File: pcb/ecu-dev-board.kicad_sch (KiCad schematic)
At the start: 1 part, among them J1 MX23A18NF1

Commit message: added more connector tags
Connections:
- net MAP_SW: now reaches J1.14
- net COIL_QS: now reaches J1.16
- net +12V: now reaches J1.3
- net DIGITAL_QS_IN: now reaches J1.4
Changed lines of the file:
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@@
+	(wire
+		(pts
+			(xy 53.34 171.45) (xy 55.88 171.45)
+		)
+		(stroke
+			(width 0)
+			(type default)
+		)
+	)
 	(wire
 		(pts
@@
 	(wire
 		(pts
+			(xy 81.28 179.07) (xy 78.74 179.07)
+		)
+		(stroke
+			(width 0)
+			(type default)
+		)
+	)
+	(wire
+		(pts
+			(xy 46.99 168.91) (xy 55.88 168.91)
+		)
+		(stroke
+			(width 0)
+			(type default)
+		)
+	)
+	(wire
+		(pts
 			(xy 46.99 166.37) (xy 55.88 166.37)
 		)
@@
 	(wire
 		(pts
+			(xy 81.28 173.99) (xy 78.74 173.99)
+		)
+		(stroke
+			(width 0)
+			(type default)
+		)
+	)
+	(wire
+		(pts
 			(xy 81.28 166.37) (xy 78.74 166.37)
 		)
@@
 		)
 	)
+	(global_label "DIGITAL_QS_IN"
+		(shape input)
+		(at 53.34 171.45 180)
+		(fields_autoplaced yes)
+		(effects
+			(font
+				(size 1.27 1.27)
+			)
+			(justify right)
+		)
+		(property "Intersheetrefs" "${INTERSHEET_REFS}"
+			(at 37.1104 171.45 0)
+			(effects
+				(font
+					(size 1.27 1.27)
+				)
+				(justify right)
+				(hide yes)
+			)
+		)
+	)
 	(global_label "KILL_SWITCH"
 		(shape input)
@@
 		)
 	)
+	(global_label "COIL_QS"
+		(shape input)
+		(at 81.28 179.07 0)
+		(fields_autoplaced yes)
+		(effects
+			(font
+				(size 1.27 1.27)
+			)
+			(justify left)
+		)
+		(property "Intersheetrefs" "${INTERSHEET_REFS}"
+			(at 92.0062 179.07 0)
+			(effects
+				(font
+					(size 1.27 1.27)
+				)
+				(justify left)
+				(hide yes)
+			)
+		)
+	)
 	(global_label "COIL"
 		(shape input)
@@
 		(property "Intersheetrefs" "${INTERSHEET_REFS}"
 			(at 91.4014 168.91 0)
+			(effects
+				(font
+					(size 1.27 1.27)
+				)
+				(justify left)
+				(hide yes)
+			)
+		)
+	)
+	(global_label "MAP_SW"
+		(shape input)
+		(at 81.28 173.99 0)
+		(fields_autoplaced yes)
+		(effects
+			(font
+				(size 1.27 1.27)
+			)
+			(justify left)
+		)
+		(property "Intersheetrefs" "${INTERSHEET_REFS}"
+			(at 91.7037 173.99 0)
 			(effects
 				(font
@@
 					(unit 1)
 				)
+			)
+		)
+	)
+	(symbol
+		(lib_id "power:+12V")
+		(at 46.99 168.91 90)
+		(unit 1)
+		(exclude_from_sim no)
+		(in_bom yes)
+		(on_board yes)
+		(dnp no)
+		(fields_autoplaced yes)
+		(property "Reference" "#PWR059"
+			(at 50.8 168.91 0)
+			(effects
+				(font
+					(size 1.27 1.27)
+				)
+				(hide yes)
+			)
+		)
+		(property "Value" "+12V"
+			(at 43.18 168.9099 90)
+			(effects
+				(font
+					(size 1.27 1.27)
+				)
+				(justify left)
+			)
+		)
+		(property "Footprint" ""
+			(at 46.99 168.91 0)
+			(effects
+				(font
+					(size 1.27 1.27)
+				)
+				(hide yes)
+			)
+		)
+		(property "Datasheet" ""
+			(at 46.99 168.91 0)
+			(effects
+				(font
+					(size 1.27 1.27)
+				)
+				(hide yes)
+			)
+		)
+		(property "Description" "Power symbol creates a global label with name \"+12V\""
+			(at 46.99 168.91 0)
+			(effects
+				(font
+					(size 1.27 1.27)
+				)
+				(hide yes)
+			)
+		)
+		(pin "1"
+		)
+		(instances
+			(project ""
+				(path "/38d4df77-b5a0-4642-8410-8b13c21c2c3b"
+					(reference "#PWR059")
+					(unit 1)
+				)

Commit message: enhanced pickup simulation
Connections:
- net PICKUP_SIM+: now reaches J1.8
- net PICKUP_SIM-: now reaches J1.9
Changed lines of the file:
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@@
+	(wire
+		(pts
+			(xy 53.34 184.15) (xy 55.88 184.15)
+		)
+		(stroke
+			(width 0)
+			(type default)
+		)
+	)
 	(wire
 		(pts
@@
 	(wire
 		(pts
-			(xy 44.45 179.07) (xy 55.88 179.07)
+			(xy 38.1 179.07) (xy 55.88 179.07)
 		)
 		(stroke
@@
 	(wire
 		(pts
+			(xy 53.34 181.61) (xy 55.88 181.61)
+		)
+		(stroke
+			(width 0)
+			(type default)
+		)
+	)
+	(wire
+		(pts
 			(xy 81.28 173.99) (xy 78.74 173.99)
 		)
@@
 		)
 	)
+	(global_label "PICKUP_SIM+"
+		(shape input)
+		(at 53.34 181.61 180)
+		(fields_autoplaced yes)
+		(effects
+			(font
+				(size 1.27 1.27)
+			)
+			(justify right)
+		)
+		(property "Intersheetrefs" "${INTERSHEET_REFS}"
+			(at 37.5338 181.61 0)
+			(effects
+				(font
+					(size 1.27 1.27)
+				)
+				(justify right)
+				(hide yes)
+			)
+		)
+	)
 	(global_label "SPARK"
 		(shape input)
@@
 				)
 				(justify left)
+				(hide yes)
+			)
+		)
+	)
+	(global_label "PICKUP_SIM-"
+		(shape input)
+		(at 53.34 184.15 180)
+		(fields_autoplaced yes)
+		(effects
+			(font
+				(size 1.27 1.27)
+			)
+			(justify right)
+		)
+		(property "Intersheetrefs" "${INTERSHEET_REFS}"
+			(at 37.5338 184.15 0)
+			(effects
+				(font
+					(size 1.27 1.27)
+				)
+				(justify right)
 				(hide yes)
 			)
@@
 	(symbol
 		(lib_id "power:GNDPWR")
-		(at 44.45 179.07 270)
+		(at 38.1 179.07 270)
 		(unit 1)
 		(exclude_from_sim no)
@@
 		(fields_autoplaced yes)
 		(property "Reference" "#PWR058"
-			(at 39.37 179.07 0)
+			(at 33.02 179.07 0)
 			(effects
 				(font
@@
 		)
 		(property "Value" "GNDPWR"
-			(at 40.64 178.9429 90)
+			(at 34.29 178.9429 90)
 			(effects
 				(font
@@
 		)
 		(property "Footprint" ""
-			(at 43.18 179.07 0)
+			(at 36.83 179.07 0)
 			(effects
 				(font
@@
 		)
 		(property "Datasheet" ""
-			(at 43.18 179.07 0)
+			(at 36.83 179.07 0)
 			(effects
 				(font
@@
 		)
 		(property "Description" "Power symbol creates a global label with name \"GNDPWR\" , global ground"
-			(at 44.45 179.07 0)
-			(effects
-				(font
+			(at 38.1 179.07 0)
+			(effects
+				(font

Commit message: changed SCR drives to pnp drive and started schematic revision
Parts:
- J1: footprint MX23A18NF1 -> SamacSys_Parts:MX23A18NF1
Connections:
- net ENABLE_QS: now reaches J1.15
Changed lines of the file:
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@@
+	(wire
+		(pts
+			(xy 81.28 176.53) (xy 78.74 176.53)
+		)
+		(stroke
+			(width 0)
+			(type default)
+		)
+	)
 	(wire
 		(pts
@@
 			(width 0)
 			(type default)
+		)
+	)
+	(global_label "ENABLE_QS"
+		(shape input)
+		(at 81.28 176.53 0)
+		(fields_autoplaced yes)
+		(effects
+			(font
+				(size 1.27 1.27)
+			)
+			(justify left)
+		)
+		(property "Intersheetrefs" "${INTERSHEET_REFS}"
+			(at 94.788 176.53 0)
+			(effects
+				(font
+					(size 1.27 1.27)
+				)
+				(justify left)
+				(hide yes)
+			)
 		)
 	)
@@
 			)
 		)
-		(property "Footprint" "MX23A18NF1"
+		(property "Footprint" "SamacSys_Parts:MX23A18NF1"
 			(at 74.93 161.29 0)
 			(effects

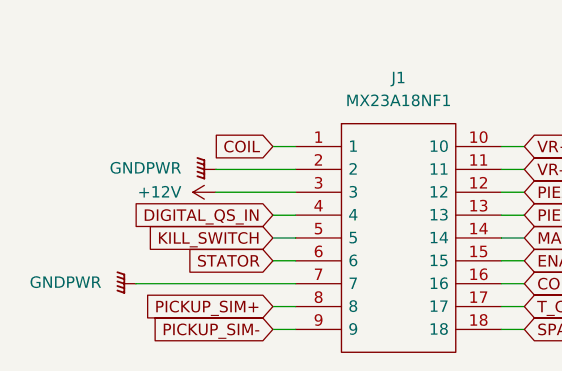
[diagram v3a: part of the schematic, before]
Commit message: added PSU status LEDs and stator winding support
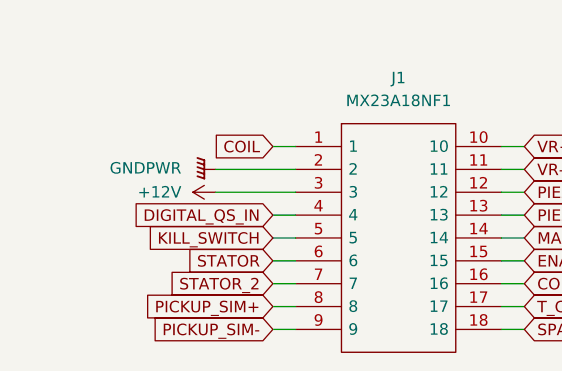
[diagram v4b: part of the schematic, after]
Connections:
- net GNDPWR: no longer J1.7
- new net STATOR_2: J1.7
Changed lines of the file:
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@@
 	(wire
 		(pts
-			(xy 38.1 179.07) (xy 55.88 179.07)
+			(xy 53.34 179.07) (xy 55.88 179.07)
 		)
 		(stroke
@@
 		(property "Intersheetrefs" "${INTERSHEET_REFS}"
 			(at 43.521 176.53 0)
+			(effects
+				(font
+					(size 1.27 1.27)
+				)
+				(justify right)
+				(hide yes)
+			)
+		)
+	)
+	(global_label "STATOR_2"
+		(shape input)
+		(at 53.34 179.07 180)
+		(fields_autoplaced yes)
+		(effects
+			(font
+				(size 1.27 1.27)
+			)
+			(justify right)
+		)
+		(property "Intersheetrefs" "${INTERSHEET_REFS}"
+			(at 41.3439 179.07 0)
 			(effects
 				(font
@@
 					(unit 1)
 				)
-			)
-		)
-	)
-	(symbol
-		(lib_id "power:GNDPWR")
-		(at 38.1 179.07 270)
-		(unit 1)
-		(exclude_from_sim no)
-		(in_bom yes)
-		(on_board yes)
-		(dnp no)
-		(fields_autoplaced yes)
-		(property "Reference" "#PWR058"
-			(at 33.02 179.07 0)
-			(effects
-				(font
-					(size 1.27 1.27)
-				)
-				(hide yes)
-			)
-		)
-		(property "Value" "GNDPWR"
-			(at 34.29 178.9429 90)
-			(effects
-				(font
-					(size 1.27 1.27)
-				)
-				(justify right)
-			)
-		)
-		(property "Footprint" ""
-			(at 36.83 179.07 0)
-			(effects
-				(font
-					(size 1.27 1.27)
-				)
-				(hide yes)
-			)
-		)
-		(property "Datasheet" ""
-			(at 36.83 179.07 0)
-			(effects
-				(font
-					(size 1.27 1.27)
-				)
-				(hide yes)
-			)
-		)
-		(property "Description" "Power symbol creates a global label with name \"GNDPWR\" , global ground"
-			(at 38.1 179.07 0)
-			(effects
-				(font
-					(size 1.27 1.27)
-				)
-				(hide yes)
-			)
-		)
-		(pin "1"
-		)
-		(instances
-			(project "ecu-dev-board"
-				(path "/38d4df77-b5a0-4642-8410-8b13c21c2c3b"
-					(reference "#PWR058")
-					(unit 1)
-				)

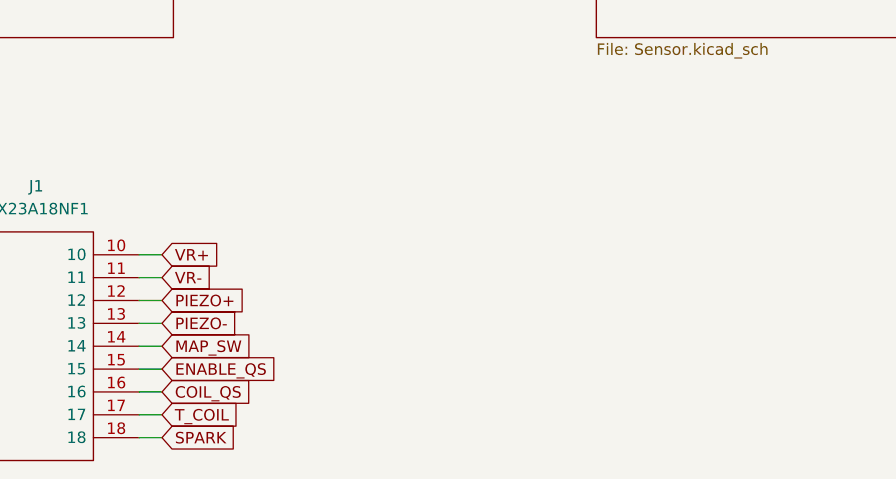
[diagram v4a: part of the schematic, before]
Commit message: added DNP for fabrication and 2P molex connector, minor fixes
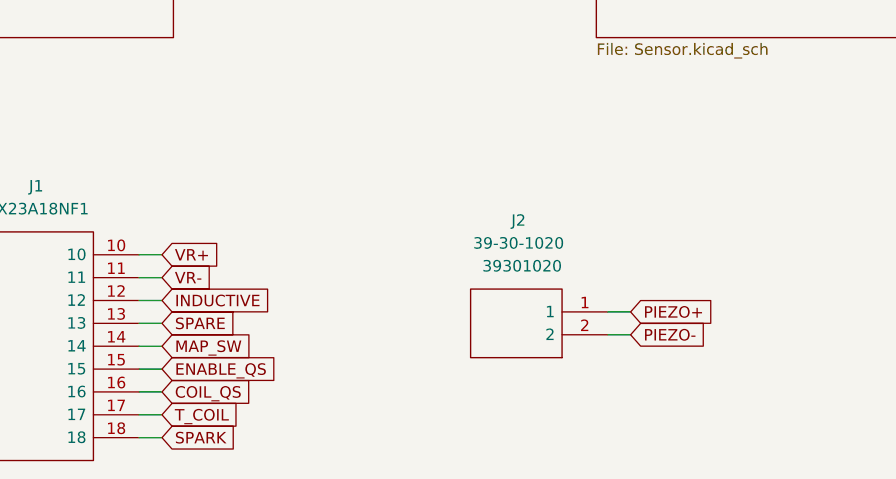
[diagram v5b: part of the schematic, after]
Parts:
- added J2: 39-30-1020, Custom:Molex_Mini-Fit_Jr_5569-02A2_2x01_P4.20mm_Horizontal, symbol SamacSys_Parts:39-30-1020
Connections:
- net PIEZO+: now also J2.1; no longer J1.12
- net PIEZO-: now also J2.2; no longer J1.13
- new net INDUCTIVE: J1.12
- new net SPARE: J1.13
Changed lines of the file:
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@@
+	(wire
+		(pts
+			(xy 133.35 172.72) (xy 130.81 172.72)
+		)
+		(stroke
+			(width 0)
+			(type default)
+		)
+	)
 	(wire
 		(pts
@@
 	(wire
 		(pts
+			(xy 133.35 170.18) (xy 130.81 170.18)
+		)
+		(stroke
+			(width 0)
+			(type default)
+		)
+	)
+	(wire
+		(pts
 			(xy 53.34 181.61) (xy 55.88 181.61)
 		)
@@
 		)
 	)
+	(global_label "INDUCTIVE"
+		(shape input)
+		(at 81.28 168.91 0)
+		(fields_autoplaced yes)
+		(effects
+			(font
+				(size 1.27 1.27)
+			)
+			(justify left)
+		)
+		(property "Intersheetrefs" "${INTERSHEET_REFS}"
+			(at 93.881 168.91 0)
+			(effects
+				(font
+					(size 1.27 1.27)
+				)
+				(justify left)
+				(hide yes)
+			)
+		)
+	)
 	(global_label "ENABLE_QS"
 		(shape input)
@@
 		)
 	)
+	(global_label "PIEZO+"
+		(shape input)
+		(at 133.35 170.18 0)
+		(fields_autoplaced yes)
+		(effects
+			(font
+				(size 1.27 1.27)
+			)
+			(justify left)
+		)
+		(property "Intersheetrefs" "${INTERSHEET_REFS}"
+			(at 143.4714 170.18 0)
+			(effects
+				(font
+					(size 1.27 1.27)
+				)
+				(justify left)
+				(hide yes)
+			)
+		)
+	)
 	(global_label "KILL_SWITCH"
 		(shape input)
@@
 		)
 	)
+	(global_label "SPARE"
+		(shape input)
+		(at 81.28 171.45 0)
+		(fields_autoplaced yes)
+		(effects
+			(font
+				(size 1.27 1.27)
+			)
+			(justify left)
+		)
+		(property "Intersheetrefs" "${INTERSHEET_REFS}"
+			(at 90.2523 171.45 0)
+			(effects
+				(font
+					(size 1.27 1.27)
+				)
+				(justify left)
+				(hide yes)
+			)
+		)
+	)
 	(global_label "PICKUP_SIM+"
 		(shape input)
@@
 		)
 	)
+	(global_label "PIEZO-"
+		(shape input)
+		(at 133.35 172.72 0)
+		(fields_autoplaced yes)
+		(effects
+			(font
+				(size 1.27 1.27)
+			)
+			(justify left)
+		)
+		(property "Intersheetrefs" "${INTERSHEET_REFS}"
+			(at 143.4714 172.72 0)
+			(effects
+				(font
+					(size 1.27 1.27)
+				)
+				(justify left)
+				(hide yes)
+			)
+		)
+	)
 	(global_label "STATOR_2"
 		(shape input)
@@
 		)
 	)
-	(global_label "PIEZO+"
-		(shape input)
-		(at 81.28 168.91 0)
+	(global_label "MAP_SW"
+		(shape input)
+		(at 81.28 173.99 0)
 		(fields_autoplaced yes)
 		(effects
@@
 		)
 		(property "Intersheetrefs" "${INTERSHEET_REFS}"
-			(at 91.4014 168.91 0)
-			(effects
-				(font
-					(size 1.27 1.27)
-				)
-				(justify left)
-				(hide yes)
-			)
-		)
-	)
-	(global_label "MAP_SW"
-		(shape input)
-		(at 81.28 173.99 0)
+			(at 91.7037 173.99 0)
+			(effects
+				(font
+					(size 1.27 1.27)
+				)
+				(justify left)
+				(hide yes)
+			)
+		)
+	)
+	(global_label "VR-"
+		(shape input)
+		(at 81.28 166.37 0)
 		(fields_autoplaced yes)
 		(effects
@@
 		)
 		(property "Intersheetrefs" "${INTERSHEET_REFS}"
-			(at 91.7037 173.99 0)
-			(effects
-				(font
-					(size 1.27 1.27)
-				)
-				(justify left)
-				(hide yes)
-			)
-		)
-	)
-	(global_label "VR-"
-		(shape input)
-		(at 81.28 166.37 0)
-		(fields_autoplaced yes)
-		(effects
-			(font
-				(size 1.27 1.27)
-			)
-			(justify left)
-		)
-		(property "Intersheetrefs" "${INTERSHEET_REFS}"
 			(at 88.1962 166.37 0)
-			(effects
-				(font
-					(size 1.27 1.27)
-				)
-				(justify left)
-				(hide yes)
-			)
-		)
-	)
-	(global_label "PIEZO-"
-		(shape input)
-		(at 81.28 171.45 0)
-		(fields_autoplaced yes)
-		(effects
-			(font
-				(size 1.27 1.27)
-			)
-			(justify left)
-		)
-		(property "Intersheetrefs" "${INTERSHEET_REFS}"
-			(at 91.4014 171.45 0)
 			(effects
 				(font
@@
 					(unit 1)
 				)
+			)
+		)
+	)
+	(symbol
+		(lib_id "SamacSys_Parts:39-30-1020")
+		(at 130.81 172.72 180)
+		(unit 1)
+		(exclude_from_sim no)
+		(in_bom yes)
+		(on_board yes)
+		(dnp no)
+		(property "Reference" "J2"
+			(at 120.904 160.02 0)
+			(effects
+				(font
+					(size 1.27 1.27)
+				)
+			)
+		)
+		(property "Value" "39-30-1020"
+			(at 120.904 162.56 0)
+			(effects
+				(font
+					(size 1.27 1.27)
+				)
+			)
+		)
+		(property "Footprint" "Custom:Molex_Mini-Fit_Jr_5569-02A2_2x01_P4.20mm_Horizontal"
+			(at 114.3 175.26 0)
+			(effects
+				(font
+					(size 1.27 1.27)
+				)
+				(justify left)
+				(hide yes)
+			)
+		)
+		(property "Datasheet" "https://www.molex.com/pdm_docs/sd/039300020_sd.pdf"
+			(at 114.3 172.72 0)
+			(effects
+				(font
+					(size 1.27 1.27)
+				)
+				(justify left)
+				(hide yes)
+			)
+		)
+		(property "Description" "Mini-Fit Jr. Header, Dual Row, Right-Angle, with Snap-in Plastic Peg PCB Lock, 2 Circuits, PA Polyamide Nylon 6/6 94V-0"
+			(at 130.81 172.72 0)
+			(effects
+				(font
+					(size 1.27 1.27)
+				)
+				(hide yes)
+			)
+		)
+		(property "Description_1" "Mini-Fit Jr. Header, Dual Row, Right-Angle, with Snap-in Plastic Peg PCB Lock, 2 Circuits, PA Polyamide Nylon 6/6 94V-0"
+			(at 114.3 170.18 0)
+			(effects
+				(font
+					(size 1.27 1.27)
+				)
+				(justify left)
+				(hide yes)
+			)
+		)
+		(property "Height" "10"
+			(at 114.3 167.64 0)
+			(effects
+				(font
+					(size 1.27 1.27)
+				)
+				(justify left)
+				(hide yes)
+			)
+		)
+		(property "Manufacturer_Name" "Molex"
+			(at 114.3 165.1 0)
+			(effects
+				(font
+					(size 1.27 1.27)
+				)
+				(justify left)
+				(hide yes)
+			)
+		)
+		(property "Manufacturer_Part_Number" " 39301020"
+			(at 125.73 165.1 0)
+			(effects
+				(font
+					(size 1.27 1.27)
+				)
+				(justify left)
+			)
+		)
+		(property "Mouser Part Number" "538-39-30-1020"
+			(at 114.3 160.02 0)
+			(effects
+				(font
+					(size 1.27 1.27)
+				)
+				(justify left)
+				(hide yes)
+			)
+		)
+		(property "Mouser Price/Stock" "https://www.mouser.co.uk/ProductDetail/Molex/39-30-1020?qs=tRPrwvvr%2Fuj45jNVCpHEJA%3D%3D"
+			(at 114.3 157.48 0)
+			(effects
+				(font
+					(size 1.27 1.27)
+				)
+				(justify left)
+				(hide yes)
+			)
+		)
+		(property "Arrow Part Number" ""
+			(at 114.3 154.94 0)
+			(effects
+				(font
+					(size 1.27 1.27)
+				)
+				(justify left)
+				(hide yes)
+			)
+		)
+		(property "Arrow Price/Stock" ""
+			(at 114.3 152.4 0)
+			(effects
+				(font
+					(size 1.27 1.27)
+				)
+				(justify left)
+				(hide yes)
+			)
+		)
+		(pin "1"
+		)
+		(pin "2"
+		)
+		(instances
+			(project ""
+				(path "/38d4df77-b5a0-4642-8410-8b13c21c2c3b"
+					(reference "J2")
+					(unit 1)
+				)

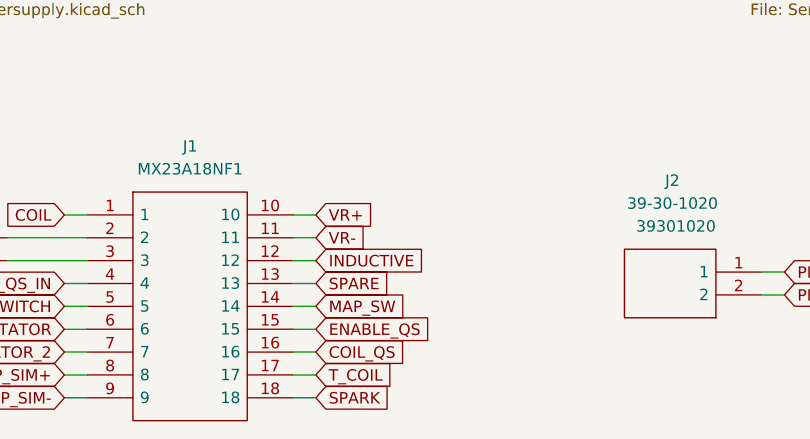
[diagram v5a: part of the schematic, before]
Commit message: added another CDI output sensing (opto coupler)
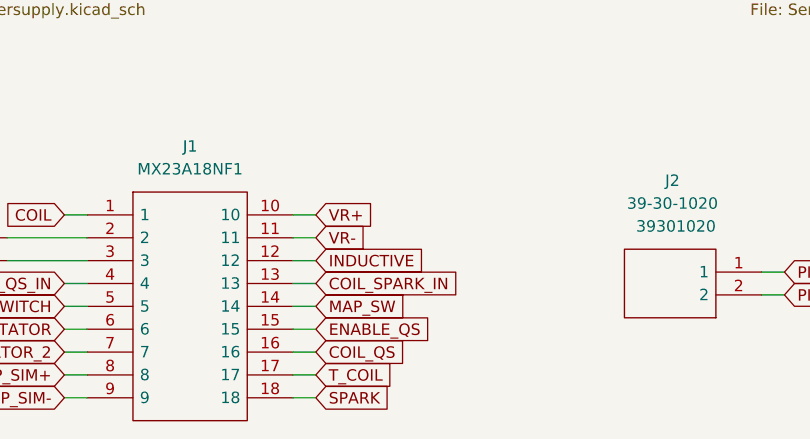
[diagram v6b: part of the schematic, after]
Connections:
- net SPARE renamed COIL_SPARK_IN
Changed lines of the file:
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@@
-		)
-	)
-	(global_label "SPARE"
-		(shape input)
-		(at 81.28 171.45 0)
-		(fields_autoplaced yes)
-		(effects
-			(font
-				(size 1.27 1.27)
-			)
-			(justify left)
-		)
-		(property "Intersheetrefs" "${INTERSHEET_REFS}"
-			(at 90.2523 171.45 0)
-			(effects
-				(font
-					(size 1.27 1.27)
-				)
-				(justify left)
-				(hide yes)
-			)
 		)
 	)
@@
 			(effects
 				(font
+					(size 1.27 1.27)
+				)
+				(justify left)
+				(hide yes)
+			)
+		)
+	)
+	(global_label "COIL_SPARK_IN"
+		(shape input)
+		(at 81.28 171.45 0)
+		(fields_autoplaced yes)
+		(effects
+			(font
+				(size 1.27 1.27)
+			)
+			(justify left)
+		)
+		(property "Intersheetrefs" "${INTERSHEET_REFS}"
+			(at 98.4772 171.45 0)
+			(effects
+				(font

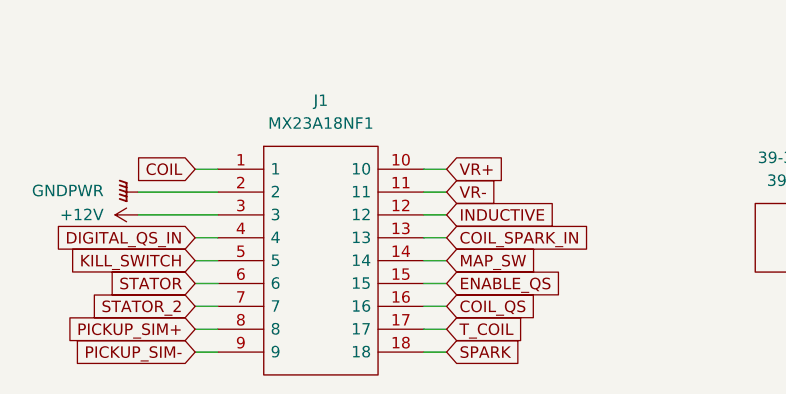
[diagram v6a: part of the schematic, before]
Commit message: made some re-routing to reduce EMI
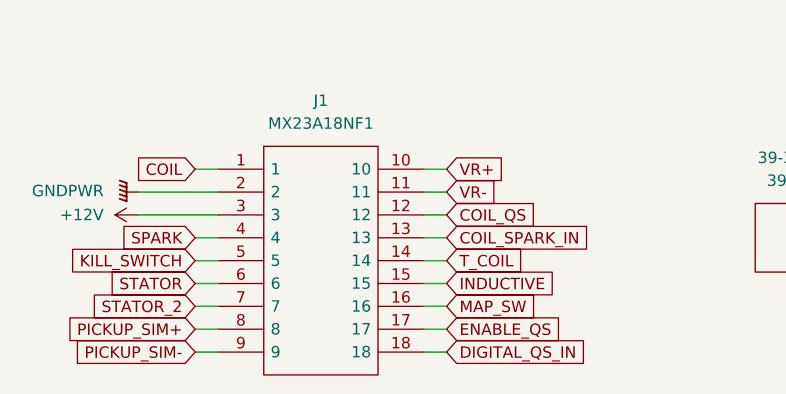
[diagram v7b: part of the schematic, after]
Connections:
- net COIL_QS: now also J1.12; no longer J1.16
- net DIGITAL_QS_IN: now also J1.18; no longer J1.4
- net ENABLE_QS: now also J1.17; no longer J1.15
- net INDUCTIVE: now also J1.15; no longer J1.12
- net MAP_SW: now also J1.16; no longer J1.14
- net SPARK: now also J1.4; no longer J1.18
- net T_COIL: now also J1.14; no longer J1.17
